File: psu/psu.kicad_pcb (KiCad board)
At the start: 2 copper layers, 26.5 x 20 mm, 17 parts, among them J1 Screw_Terminal_01x02, J2 Screw_Terminal_01x02

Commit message: made the pcb , It's a bit trash but still need to make a q&a document
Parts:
- NT1: moved to B.Cu
- moved R7 16.8 mm to (143.5, 86.5), turned to 90 degrees
- moved R2 15.1 mm to (141.0, 89.0), turned to 90 degrees
- moved R5 12.7 mm to (140.0, 89.5), turned to -90 degrees
- moved R4 10.2 mm to (137.1, 89.2)
- moved R1 7.83 mm to (134.5, 84.0), turned to -90 degrees
- moved R3 7.42 mm to (134.5, 82.0), turned to -90 degrees
- moved J1 6.57 mm to (146.8, 77.5)
- moved D1 6.35 mm to (140.2, 90.8), turned to 180 degrees
- moved NT1 6.16 mm to (140.2, 85.2), turned to 90 degrees
- moved R6 2.69 mm to (143.5, 89.0), turned to -90 degrees
- moved J2 2.00 mm to (137.7, 73.2)
- moved C1 1.51 mm to (143.5, 84.1)
- moved C2 1.51 mm to (145.5, 84.1)
- moved U1 1.51 mm to (139.0, 84.3)
- moved C4 1.25 mm to (138.5, 79.2)
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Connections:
- net Net-(J1-Pin_2) renamed /Vin
- net Net-(J2-Pin_1) renamed /Vout
- net Net-(U1-EN) renamed /EN
- net Net-(U1-FB) renamed /FB
- net Net-(U1-PG) renamed /PG
- net Net-(U1-RT) renamed /RT
- net Net-(U1-VCC) renamed /VCC
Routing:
- net /EN: track 0.00 -> 4.77 mm
- net AGND: track 0.00 -> 4.38 mm, vias 0 -> 3
- net /Vout: track 0.00 -> 3.88 mm
- net PGND: track 0.00 -> 3.82 mm, vias 0 -> 6
- net /VCC: track 0.00 -> 3.08 mm
- net /PG: track 0.00 -> 1.97 mm
- net /RT: track 0.00 -> 1.86 mm
- net /FB: track 0.00 -> 1.19 mm
- added copper zone on F.Cu, net /Vin
- added copper zone on F.Cu, net /Vout
- added copper zone on B.Cu, net AGND
- added copper zone on B.Cu, net PGND
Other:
- board size 26.5 x 20 mm -> 14.8 x 19.8 mm

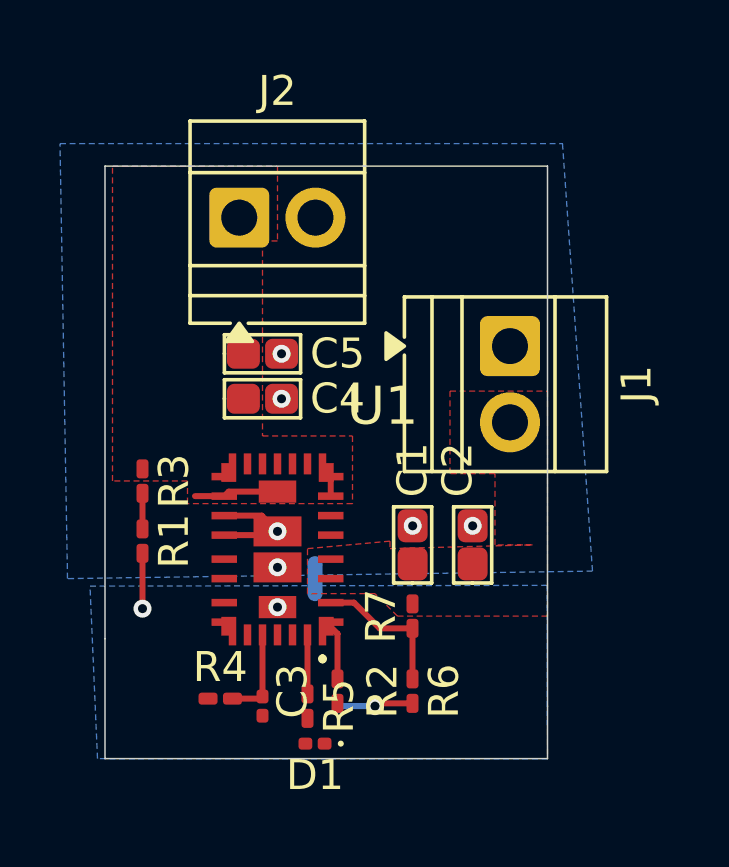
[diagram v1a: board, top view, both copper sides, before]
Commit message: finished
finished the schematic , bom and rough pcb outline
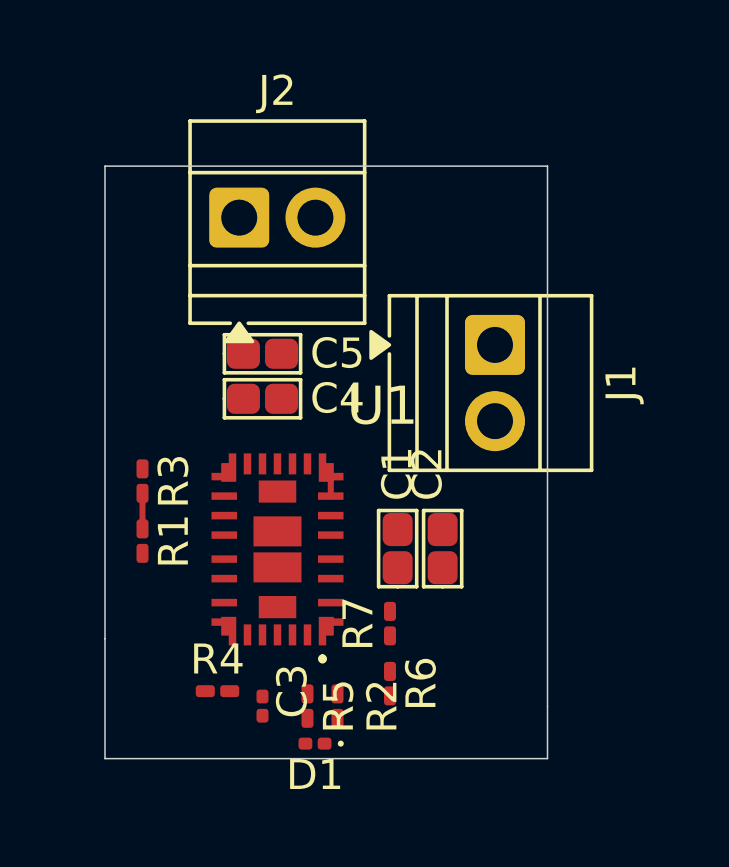
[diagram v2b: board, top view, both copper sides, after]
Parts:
- removed NT1: NetTie_2, NetTie:NetTie-2_SMD_Pad0.5mm
- moved C2 1.01 mm to (144.5, 84.2)
- moved R6 0.79 mm to (142.8, 88.8)
- moved R7 0.79 mm to (142.8, 86.8)
- moved C1 0.52 mm to (143.0, 84.2)
- moved J1 0.50 mm to (146.2, 77.5)
- moved R2 0.50 mm to (141.0, 89.5)
- moved R4 0.27 mm to (137.0, 89.0)
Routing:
- net /EN: track 4.77 -> 0.00 mm
- net AGND: track 4.38 -> 0.00 mm, vias 3 -> 0
- net PGND: track 3.82 -> 0.18 mm, vias 6 -> 0
- net /VCC: track 3.08 -> 0.10 mm
- net /Vout: track 3.88 -> 1.06 mm
- net /PG: track 1.97 -> 0.00 mm
- net /RT: track 1.86 -> 0.00 mm
- removed copper zone on F.Cu, net /Vin
- removed copper zone on F.Cu, net /Vout
- removed copper zone on B.Cu, net AGND
- removed copper zone on B.Cu, net PGND
